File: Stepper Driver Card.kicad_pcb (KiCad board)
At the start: 2 copper layers, 101.6 x 68.6 mm, 38 parts, among them J1 Conn_02x22_Top_Bottom, J2 Conn_01x03, J3 Conn_01x03, J4 Conn_01x03, J5 Conn_01x04, J6 Conn_01x04, Q1 STD20NF06L, Q2 STD20NF06L, Q3 STD20NF06L, Q4 STD20NF06L, Q5 STD20NF06L, Q6 STD20NF06L, Q7 STD20NF06L, Q8 STD20NF06L, U2 STM32F030C8Tx, U3 DRV8711

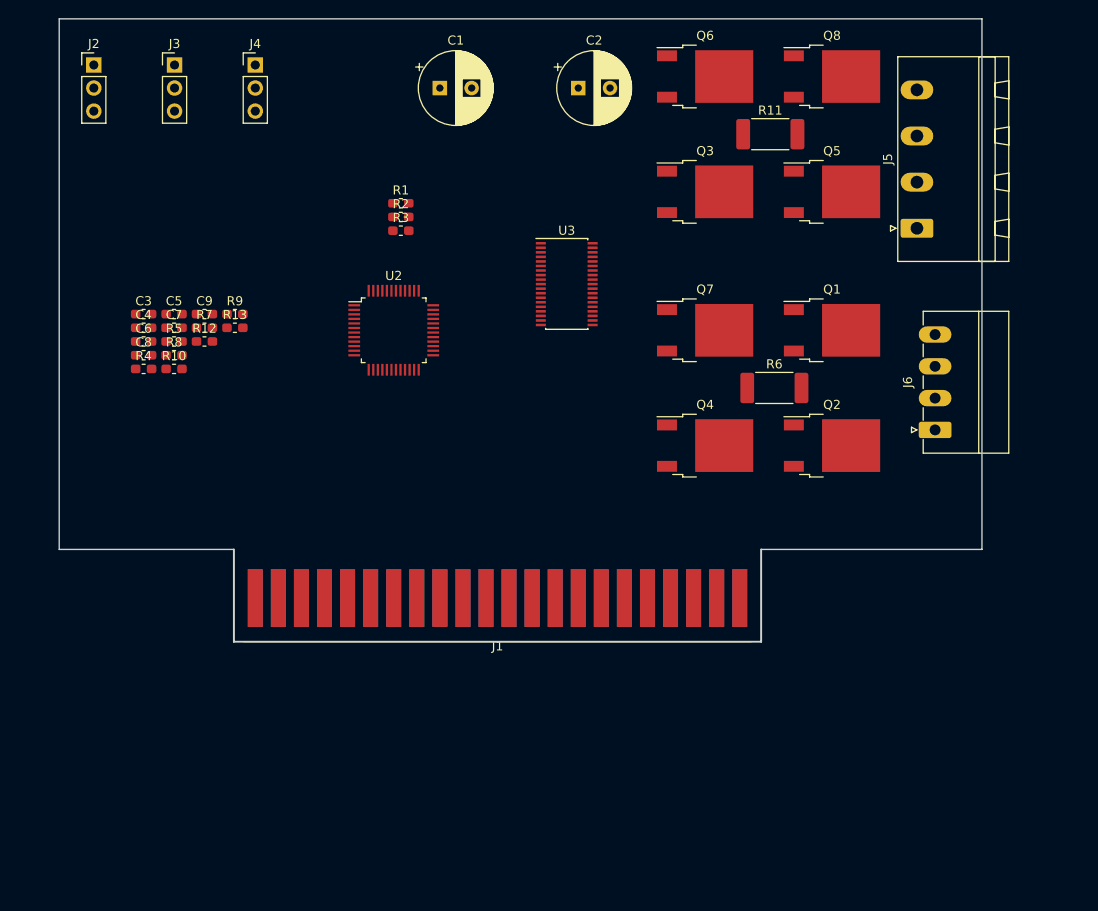
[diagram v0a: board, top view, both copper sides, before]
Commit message: worked on motor driver layout
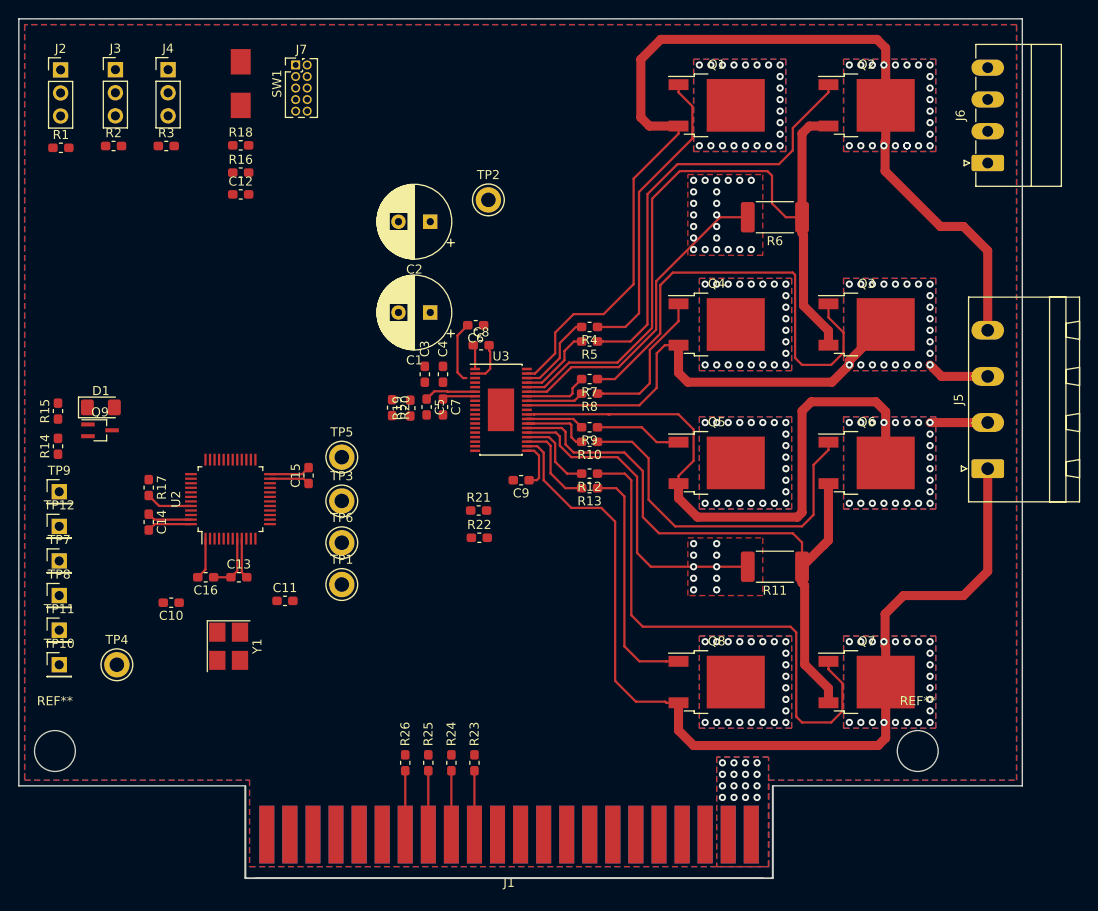
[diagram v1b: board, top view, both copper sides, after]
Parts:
- added C10: 18pF, Capacitor_SMD:C_0603_1608Metric_Pad1.05x0.95mm_HandSolder, F.Cu at (98.7, 117.6)
- added C11: 18pF, Capacitor_SMD:C_0603_1608Metric_Pad1.05x0.95mm_HandSolder, F.Cu at (111.2, 117.4)
- added C12: 0.1uF, Capacitor_SMD:C_0603_1608Metric_Pad1.05x0.95mm_HandSolder, F.Cu at (106.3, 72.7)
- added C13: 0.1uF, Capacitor_SMD:C_0603_1608Metric_Pad1.05x0.95mm_HandSolder, F.Cu at (106.1, 114.8)
- added C14: 0.1uF, Capacitor_SMD:C_0603_1608Metric_Pad1.05x0.95mm_HandSolder, F.Cu at (96.2, 108.8)
- added C15: 0.1uF, Capacitor_SMD:C_0603_1608Metric_Pad1.05x0.95mm_HandSolder, F.Cu at (113.8, 103.6)
- added C16: 0.1uF, Capacitor_SMD:C_0603_1608Metric_Pad1.05x0.95mm_HandSolder, F.Cu at (102.5, 114.8)
- added D1: LED, LED_SMD:LED_1206_3216Metric_Pad1.42x1.75mm_HandSolder, F.Cu at (90.9, 96.1)
- added J7: Conn_02x05_Odd_Even, Connector_PinHeader_1.27mm:PinHeader_2x05_P1.27mm_Vertical, F.Cu at (112.4, 58.4)
- added Q9: Q_NMOS_GSD, Package_TO_SOT_SMD:SOT-323_SC-70_Handsoldering, F.Cu at (90.9, 98.6)
- added R14: 10K, Resistor_SMD:R_0603_1608Metric_Pad1.05x0.95mm_HandSolder, F.Cu at (86.2, 100.4)
- added R15: 10K, Resistor_SMD:R_0603_1608Metric_Pad1.05x0.95mm_HandSolder, F.Cu at (86.2, 96.5)
- added R16: 10K, Resistor_SMD:R_0603_1608Metric_Pad1.05x0.95mm_HandSolder, F.Cu at (106.3, 70.3)
- added R17: 10K, Resistor_SMD:R_0603_1608Metric_Pad1.05x0.95mm_HandSolder, F.Cu at (96.2, 105.0)
- added R18: 10K, Resistor_SMD:R_0603_1608Metric_Pad1.05x0.95mm_HandSolder, F.Cu at (106.3, 67.3)
- added R19: 10K, Resistor_SMD:R_0603_1608Metric_Pad1.05x0.95mm_HandSolder, F.Cu at (125.0, 96.2)
- added R20: 10K, Resistor_SMD:R_0603_1608Metric_Pad1.05x0.95mm_HandSolder, F.Cu at (123.0, 96.2)
- added R21: 10K, Resistor_SMD:R_0603_1608Metric_Pad1.05x0.95mm_HandSolder, F.Cu at (132.5, 107.5)
- added R22: 10K, Resistor_SMD:R_0603_1608Metric_Pad1.05x0.95mm_HandSolder, F.Cu at (132.6, 110.5)
- added R23: 0R, Resistor_SMD:R_0603_1608Metric_Pad1.05x0.95mm_HandSolder, F.Cu at (132.1, 135.3)
- added R24: 0R, Resistor_SMD:R_0603_1608Metric_Pad1.05x0.95mm_HandSolder, F.Cu at (129.5, 135.3)
- added R25: 0R, Resistor_SMD:R_0603_1608Metric_Pad1.05x0.95mm_HandSolder, F.Cu at (127.0, 135.3)
- added R26: 0R, Resistor_SMD:R_0603_1608Metric_Pad1.05x0.95mm_HandSolder, F.Cu at (124.5, 135.3)
- added REF**: MountingHole_4.5mm, MountingHole:MountingHole_4.5mm, F.Cu at (180.9, 134.0)
- added REF**: MountingHole_4.5mm, MountingHole:MountingHole_4.5mm, F.Cu at (85.9, 134.0)
- added SW1: SW_Push, switches_mdg:FSM2JMTR, F.Cu at (106.3, 60.5)
- added TP1: TestPoint, test_points_mdg:Keystone_5010, F.Cu at (117.5, 115.6)
- added TP10: TestPoint, Connector_PinHeader_2.54mm:PinHeader_1x01_P2.54mm_Vertical, F.Cu at (86.4, 124.5)
- added TP11: TestPoint, Connector_PinHeader_2.54mm:PinHeader_1x01_P2.54mm_Vertical, F.Cu at (86.4, 120.7)
- added TP12: TestPoint, Connector_PinHeader_2.54mm:PinHeader_1x01_P2.54mm_Vertical, F.Cu at (86.4, 109.2)
- added TP2: TestPoint, test_points_mdg:Keystone_5010, F.Cu at (133.6, 73.3)
- added TP3: TestPoint, test_points_mdg:Keystone_5010, F.Cu at (117.5, 106.4)
- added TP4: TestPoint, test_points_mdg:Keystone_5010, F.Cu at (92.7, 124.5)
- added TP5: TestPoint, test_points_mdg:Keystone_5010, F.Cu at (117.5, 101.6)
- added TP6: TestPoint, test_points_mdg:Keystone_5010, F.Cu at (117.5, 111.0)
- added TP7: TestPoint, Connector_PinHeader_2.54mm:PinHeader_1x01_P2.54mm_Vertical, F.Cu at (86.4, 113.0)
- added TP8: TestPoint, Connector_PinHeader_2.54mm:PinHeader_1x01_P2.54mm_Vertical, F.Cu at (86.4, 116.8)
- added TP9: TestPoint, Connector_PinHeader_2.54mm:PinHeader_1x01_P2.54mm_Vertical, F.Cu at (86.4, 105.4)
- added Y1: Crystal_GND24, Crystal:Crystal_SMD_SeikoEpson_FA238V-4Pin_3.2x2.5mm_HandSoldering, F.Cu at (105.0, 122.4)
- U3: footprint Package_SO:TSSOP-38_4.4x9.7mm_P0.5mm -> packages_mdg:TSSOP-38-1_Power_Pad_4.4x9.7mm_P0.5mm
- moved Q8 67.9 mm to (158.8, 126.4)
- moved R4 49.3 mm to (144.8, 87.3), turned to 180 degrees
- moved R11 47.6 mm to (165.2, 113.7), turned to 180 degrees
- moved R10 46.4 mm to (144.8, 99.9), turned to 180 degrees
- moved Q6 46.1 mm to (175.3, 102.2)
- moved R8 45.9 mm to (144.8, 94.6), turned to 180 degrees
- moved R5 45.7 mm to (144.8, 88.9), turned to 180 degrees
- moved R12 44.8 mm to (144.8, 103.4), turned to 180 degrees
- moved R13 42.9 mm to (144.8, 105.0), turned to 180 degrees
- moved R7 42.8 mm to (144.8, 93.0), turned to 180 degrees
- moved Q7 42.6 mm to (175.3, 126.4)
- moved R9 41.0 mm to (144.8, 98.3), turned to 180 degrees
- moved C9 39.4 mm to (137.2, 104.1), turned to 180 degrees
- moved R1 37.9 mm to (86.5, 67.5)
- moved Q2 37.7 mm to (175.3, 62.9)
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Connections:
- net Net-(Q2-Pad3) renamed /AISENP
- net Net-(Q6-Pad3) renamed /BISENP
- net Net-(R10-Pad2) renamed /B1LS
- net Net-(R12-Pad2) renamed /B2LS
- net Net-(R13-Pad2) renamed /B2HS
- net Net-(R4-Pad2) renamed /A1HS
- net Net-(R5-Pad2) renamed /A1LS
- net Net-(R7-Pad2) renamed /A2LS
- net Net-(R8-Pad2) renamed /A2HS
- net Net-(R9-Pad2) renamed /B1HS
- net Net-(U2-Pad37) renamed /DRV_FAULT
- net Net-(U2-Pad38) renamed /DRV_STALL
- J1 pad 10: I2C_SCL -> SPI2_MISO
- J1 pad 11: I2C_ADD0 -> SPI2_MOSI
- J1 pad 12: I2C_ADD1 -> SPI2_CS
- J1 pad 13: I2C_ADD2 -> STEP
- J1 pad 14: CARD_ENABLE -> DIR
- J1 pad 15: CARD_STATUS -> BIN1
- J1 pad 16: Net-(J1-Pad16) -> BIN2
- J1 pad 17: Net-(J1-Pad17) -> NRST
- J1 pad 18: Net-(J1-Pad18) -> GPIO_0
- J1 pad 19: Net-(J1-Pad19) -> GPIO_1
- J1 pad 31: SPI_SCK -> I2C_SDA
- J1 pad 32: SPI_MISO -> I2C_SCL
- J1 pad 33: SPI_MOSI -> I2C_ADD0
- J1 pad 34: SPI_CS -> I2C_ADD1
- J1 pad 35: Net-(J1-Pad35) -> I2C_ADD2
- J1 pad 36: Net-(J1-Pad36) -> CARD_ENABLE
- J1 pad 37: Net-(J1-Pad37) -> CARD_STATUS
- J1 pad 38: Net-(J1-Pad38) -> GPIO_5
- J1 pad 39: Net-(J1-Pad39) -> GPIO_4
- J1 pad 40: Net-(J1-Pad40) -> GPIO_3
- J1 pad 41: Net-(J1-Pad41) -> GPIO_2
- J1 pad 9: I2C_SDA -> SPI2_SCK
- J5 pad 1: Net-(J5-Pad1) -> /BOUT2
- J5 pad 2: Net-(J5-Pad2) -> /BOUT1
- J5 pad 3: Net-(J5-Pad3) -> /AOUT2
- J5 pad 4: Net-(J5-Pad4) -> /AOUT1
- Q1 pad 3: Net-(J5-Pad1) -> /AOUT1
- Q2 pad 2: Net-(J5-Pad1) -> /AOUT1
- Q3 pad 2: Net-(J5-Pad2) -> /AOUT2
- Q4 pad 3: Net-(J5-Pad2) -> /AOUT2
- Q5 pad 3: Net-(J5-Pad3) -> /BOUT1
- Q6 pad 2: Net-(J5-Pad3) -> /BOUT1
- Q7 pad 2: Net-(J5-Pad4) -> /BOUT2
- Q8 pad 3: Net-(J5-Pad4) -> /BOUT2
- U2 pad 1: Net-(U2-Pad1) -> +3V3
- U2 pad 15: CARD_ENABLE -> SPI1_SCK
- U2 pad 16: CARD_STATUS -> SPI1_MISO
- U2 pad 17: AXIS_SELECT_X -> SPI1_MOSI
- U2 pad 18: Net-(U2-Pad18) -> CARD_ENABLE
- U2 pad 19: Net-(U2-Pad19) -> CARD_STATUS
- U2 pad 20: Net-(U2-Pad20) -> STATUS_LED
- U2 pad 21: Net-(U2-Pad21) -> GPIO_0
- U2 pad 23: Net-(U2-Pad23) -> GND
- U2 pad 24: Net-(U2-Pad24) -> +3V3
- U2 pad 25: Net-(U2-Pad25) -> SPI2_CS
- U2 pad 26: Net-(U2-Pad26) -> SPI2_SCK
- U2 pad 27: AXIS_LIMIT_SWITCH- -> SPI2_MISO
- U2 pad 28: AXIS_LIMIT_SWITCH+ -> SPI2_MOSI
- U2 pad 29: AXIS_SELECT_Y -> SPI1_CS
- U2 pad 30: AXIS_SELECT_Z -> /DRV_SLEEP
- U2 pad 31: Net-(U2-Pad31) -> /DRV_RESET
- U2 pad 32: Net-(U2-Pad32) -> AXIS_SELECT_X
- U2 pad 33: Net-(U2-Pad33) -> AXIS_SELECT_Y
- U2 pad 34: Net-(U2-Pad34) -> AXIS_SELECT_Z
- U2 pad 39: Net-(U2-Pad39) -> AXIS_LIMIT_SWITCH-
- U2 pad 40: Net-(U2-Pad40) -> AXIS_LIMIT_SWITCH+
- U2 pad 41: Net-(U2-Pad41) -> GPIO_5
- U2 pad 42: Net-(U2-Pad42) -> GPIO_4
- U2 pad 43: Net-(U2-Pad43) -> GPIO_3
- U2 pad 45: Net-(U2-Pad45) -> GPIO_2
- U2 pad 46: Net-(U2-Pad46) -> GPIO_1
- U2 pad 47: Net-(U2-Pad47) -> GND
- U2 pad 48: Net-(U2-Pad48) -> +3V3
- U2 pad 7: Net-(U2-Pad7) -> NRST
- U2 pad 8: Net-(U2-Pad8) -> GND
- U2 pad 9: Net-(U2-Pad9) -> +3V3
- U3 pad 14: SPI_SCK -> SPI1_SCK
- U3 pad 15: SPI_MOSI -> SPI1_MOSI
- U3 pad 16: SPI_CS -> SPI1_CS
- U3 pad 17: SPI_MISO -> SPI1_MISO
- U3 pad 21: Net-(J5-Pad4) -> /BOUT2
- U3 pad 28: Net-(J5-Pad3) -> /BOUT1
- U3 pad 30: Net-(J5-Pad2) -> /AOUT2
- U3 pad 37: Net-(J5-Pad1) -> /AOUT1
- U3 pad 8: Net-(U3-Pad8) -> /DRV_SLEEP
- U3 pad 9: Net-(U3-Pad9) -> /DRV_RESET
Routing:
- net /AOUT1: track 0.00 -> 113.1 mm, vias 0 -> 24
- net /BOUT2: track 0.00 -> 105.6 mm, vias 0 -> 22
- net GND: track 0.00 -> 87.2 mm, vias 0 -> 32
- net /AISENP: track 0.00 -> 80.1 mm
- net /BOUT1: track 0.00 -> 75.5 mm, vias 0 -> 22
- net /BISENP: track 0.00 -> 68.5 mm
- net Net-(Q7-Pad1): track 0.00 -> 59.1 mm
- net /AOUT2: track 0.00 -> 57.7 mm, vias 0 -> 22
- net Net-(Q3-Pad1): track 0.00 -> 51.3 mm
- net Net-(Q2-Pad1): track 0.00 -> 47.5 mm
- net Net-(Q6-Pad1): track 0.00 -> 39.5 mm
- net Net-(Q1-Pad1): track 0.00 -> 33.4 mm
- net Net-(Q8-Pad1): track 0.00 -> 26.5 mm
- net +3V3: track 0.00 -> 18.5 mm
- net Net-(Q4-Pad1): track 0.00 -> 16.3 mm
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- added copper zone on B.Cu, net +24V
- added copper zone on F.Cu, net +24V
- added copper zone on In2.Cu, net +24V
- added copper zone on B.Cu, net /AOUT1
- added copper zone on F.Cu, net /AOUT1
- added copper zone on B.Cu, net /AOUT2
- added copper zone on F.Cu, net /AOUT2
- added copper zone on B.Cu, net /BOUT1
- added copper zone on F.Cu, net /BOUT1
- added copper zone on B.Cu, net /BOUT2
- added copper zone on F.Cu, net /BOUT2
- added copper zone on B.Cu, net GND
- added copper zone on F.Cu, net GND
- added copper zone on In1.Cu, net GND
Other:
- board size 101.6 x 68.6 mm -> 110.5 x 94.6 mm
- copper layers 2 -> 4
- net class 24V Power added: clearance 0.3, trace_width 1, via_dia 0.8, via_drill 0.4

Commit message: All traces connected, board needs to be cleaned up.
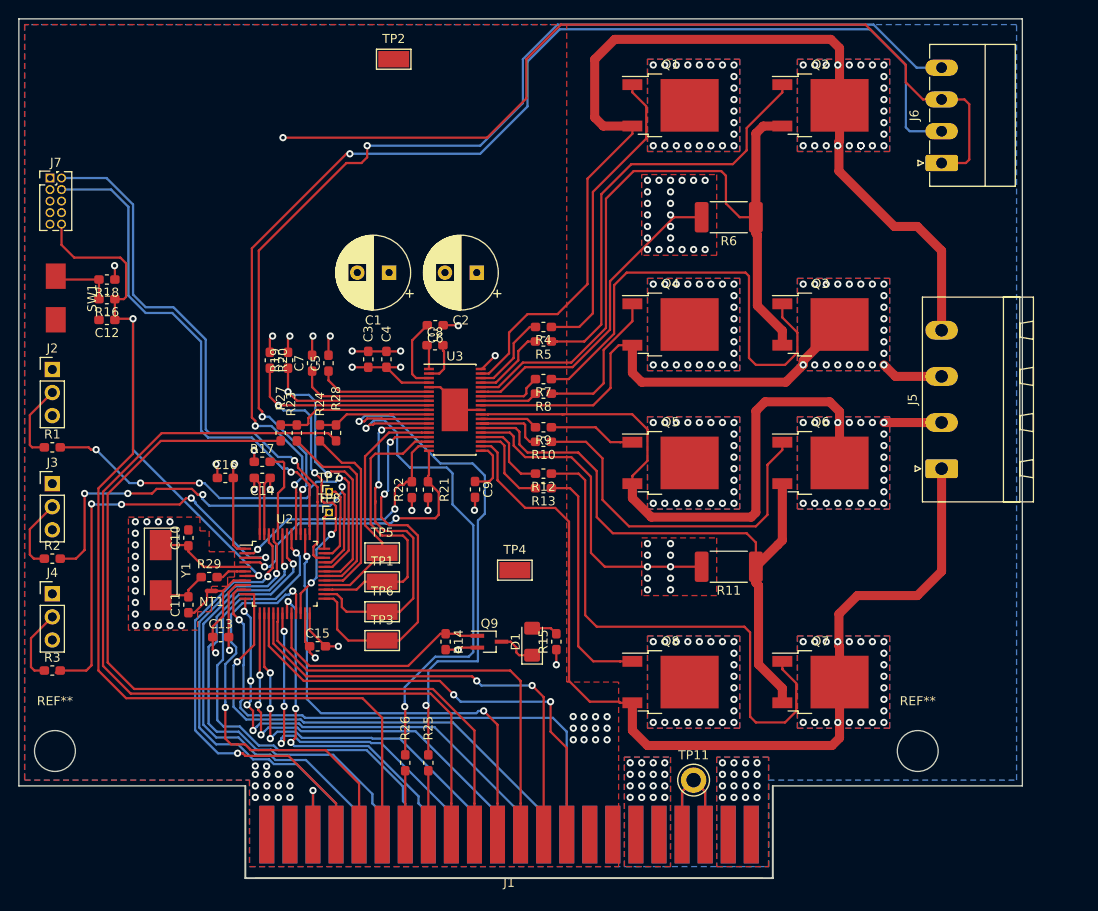
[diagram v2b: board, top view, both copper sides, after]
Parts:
- removed TP10, TP12, TP9: TestPoint, Connector_PinHeader_2.54mm:PinHeader_1x01_P2.54mm_Vertical
- added NT1: Net-Tie_2, NetTie:NetTie-2_SMD_Pad0.5mm, F.Cu at (103.1, 116.3)
- added R27: 0R, Resistor_SMD:R_0603_1608Metric_Pad1.05x0.95mm_HandSolder, F.Cu at (110.7, 98.9)
- added R28: 0R, Resistor_SMD:R_0603_1608Metric_Pad1.05x0.95mm_HandSolder, F.Cu at (116.8, 98.9)
- added R29: 10K, Resistor_SMD:R_0603_1608Metric_Pad1.05x0.95mm_HandSolder, F.Cu at (102.9, 114.8)
- TP1, TP2, TP3, TP4, TP5, TP6: footprint test_points_mdg:Keystone_5010 -> test_points_mdg:TestPoint_Keystone_5015_Micro-Minature
- TP11: footprint Connector_PinHeader_2.54mm:PinHeader_1x01_P2.54mm_Vertical -> test_points_mdg:Keystone_5010
- TP7, TP8: footprint Connector_PinHeader_2.54mm:PinHeader_1x01_P2.54mm_Vertical -> Connector_PinHeader_1.00mm:PinHeader_1x01_P1.00mm_Vertical
- Y1: value Crystal_GND24 -> Crystal; footprint Crystal:Crystal_SMD_SeikoEpson_FA238V-4Pin_3.2x2.5mm_HandSoldering -> Crystal:Crystal_SMD_Abracon_ABM3-2Pin_5.0x3.2mm_HandSoldering
- moved TP11 71.8 mm to (156.2, 137.2)
- moved R15 60.5 mm to (141.1, 121.9)
- moved R3 59.1 mm to (85.6, 125.1)
- moved J4 59.1 mm to (85.6, 116.6)
- moved D1 54.0 mm to (138.4, 121.9), turned to 90 degrees
- moved Q9 48.8 mm to (133.7, 121.9)
- moved R14 47.8 mm to (128.9, 121.9), turned to 270 degrees
- moved J3 46.1 mm to (85.6, 104.5)
- moved R2 45.9 mm to (85.6, 112.8)
- moved TP4 45.0 mm to (136.5, 114.0)
- moved R23 41.3 mm to (112.5, 98.9)
- moved R24 39.1 mm to (115.1, 98.9)
- moved J2 33.0 mm to (85.6, 91.9)
- moved R1 33.0 mm to (85.6, 100.5)
- moved SW1 31.2 mm to (86.0, 84.1)
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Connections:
- C10 pad 2: GND -> /CRYS_GND
- C11 pad 1: Net-(C11-Pad1) -> /CRYS_GND
- C11 pad 2: GND -> Net-(C11-Pad2)
- J1 pad 10: SPI2_MISO -> SPI1_MISO
- J1 pad 11: SPI2_MOSI -> SPI1_MOSI
- J1 pad 12: SPI2_CS -> SPI1_CS
- J1 pad 13: STEP -> Net-(J1-Pad13)
- J1 pad 14: DIR -> Net-(J1-Pad14)
- J1 pad 9: SPI2_SCK -> SPI1_SCK
- R20 pad 2: /DRV_RESET -> DRV_RST
- R21 pad 2: /DRV_STALL -> DRV_STALL
- R22 pad 2: /DRV_FAULT -> DRV_FAULT
- R23 pad 1: Net-(R23-Pad1) -> STEP
- R23 pad 2: STEP -> Net-(R23-Pad2)
- R24 pad 1: Net-(R24-Pad1) -> DIR
- R24 pad 2: DIR -> Net-(R24-Pad2)
- TP1 pad 1: SPI1_MISO -> SPI2_MISO
- TP11 pad 1: Net-(TP11-Pad1) -> +5V
- TP3 pad 1: SPI1_CS -> SPI2_CS
- TP5 pad 1: SPI1_MOSI -> SPI2_MOSI
- TP6 pad 1: SPI1_SCK -> SPI2_SCK
- U2 pad 2: Net-(TP9-Pad1) -> DRV_FAULT
- U2 pad 22: Net-(TP12-Pad1) -> DRV_RST
- U2 pad 29: SPI1_CS -> Net-(R24-Pad2)
- U2 pad 3: Net-(TP10-Pad1) -> AXIS_SELECT_Z
- U2 pad 30: /DRV_SLEEP -> Net-(R23-Pad2)
- U2 pad 31: /DRV_RESET -> /DRV_SLEEP
- U2 pad 34: AXIS_SELECT_Z -> SWDIO
- U2 pad 37: /DRV_FAULT -> SWCLK
- U2 pad 38: /DRV_STALL -> SPI1_CS
- U2 pad 4: Net-(TP11-Pad1) -> DRV_STALL
- U2 pad 6: Net-(C11-Pad1) -> Net-(R29-Pad2)
- U3 pad 10: Net-(R23-Pad1) -> STEP
- U3 pad 11: Net-(R24-Pad1) -> DIR
- U3 pad 14: SPI1_SCK -> SPI2_SCK
- U3 pad 15: SPI1_MOSI -> SPI2_MOSI
- U3 pad 16: SPI1_CS -> SPI2_CS
- U3 pad 17: SPI1_MISO -> SPI2_MISO
- U3 pad 18: /DRV_FAULT -> DRV_FAULT
- U3 pad 19: /DRV_STALL -> DRV_STALL
- U3 pad 9: /DRV_RESET -> DRV_RST
- Y1 pad 2: GND -> Net-(C11-Pad2)
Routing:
- net NRST: track 0.00 -> 141.7 mm, vias 0 -> 2
- net AXIS_LIMIT_SWITCH+: track 0.00 -> 132.8 mm, vias 0 -> 3
- net AXIS_LIMIT_SWITCH-: track 0.00 -> 125.1 mm, vias 0 -> 3
- net +3V3: track 18.5 -> 135.9 mm, vias 0 -> 25
- net Net-(J1-Pad14): track 0.00 -> 101.7 mm
- net Net-(J1-Pad13): track 0.00 -> 95.0 mm
- net SWDIO: track 0.00 -> 63.1 mm, vias 0 -> 1
- net I2C_SDA: track 0.00 -> 63.0 mm, vias 0 -> 1
- net Net-(R25-Pad1): track 0.00 -> 60.8 mm, vias 0 -> 2
- net Net-(R26-Pad1): track 0.00 -> 58.1 mm, vias 0 -> 2
- net SWCLK: track 0.00 -> 57.9 mm, vias 0 -> 1
- net GPIO_5: track 0.00 -> 55.8 mm, vias 0 -> 1
- net I2C_SCL: track 0.00 -> 55.6 mm, vias 0 -> 1
- net GPIO_4: track 0.00 -> 53.4 mm, vias 0 -> 1
- net SPI1_CS: track 0.00 -> 52.9 mm, vias 0 -> 2
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- added copper zone on B.Cu, net +3V3
- added copper zone on F.Cu, net +3V3
- added copper zone on In2.Cu, net +3V3
- added copper zone on F.Cu, net /CRYS_GND
- added copper zone on In1.Cu, net /CRYS_GND
